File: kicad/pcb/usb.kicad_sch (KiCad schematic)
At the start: 13 parts, among them J1 USB_C_Receptacle, U1 FE1.1, Y1 Crystal_GND23

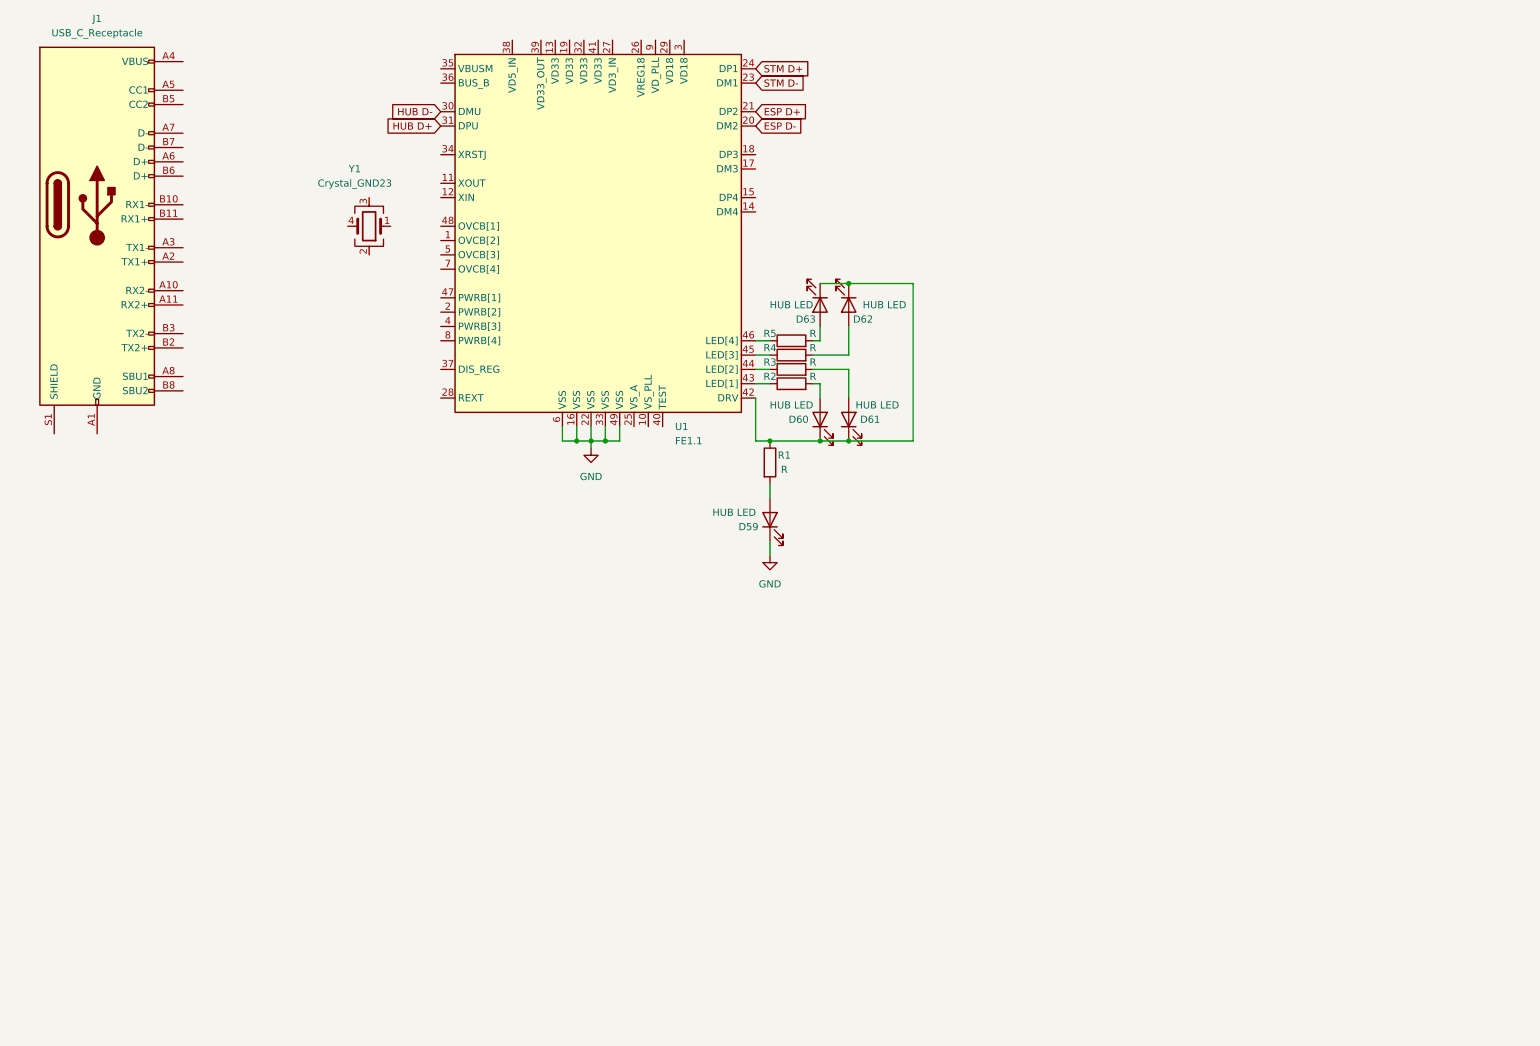
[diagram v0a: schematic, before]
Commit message: USB (almost) done + some STM progress
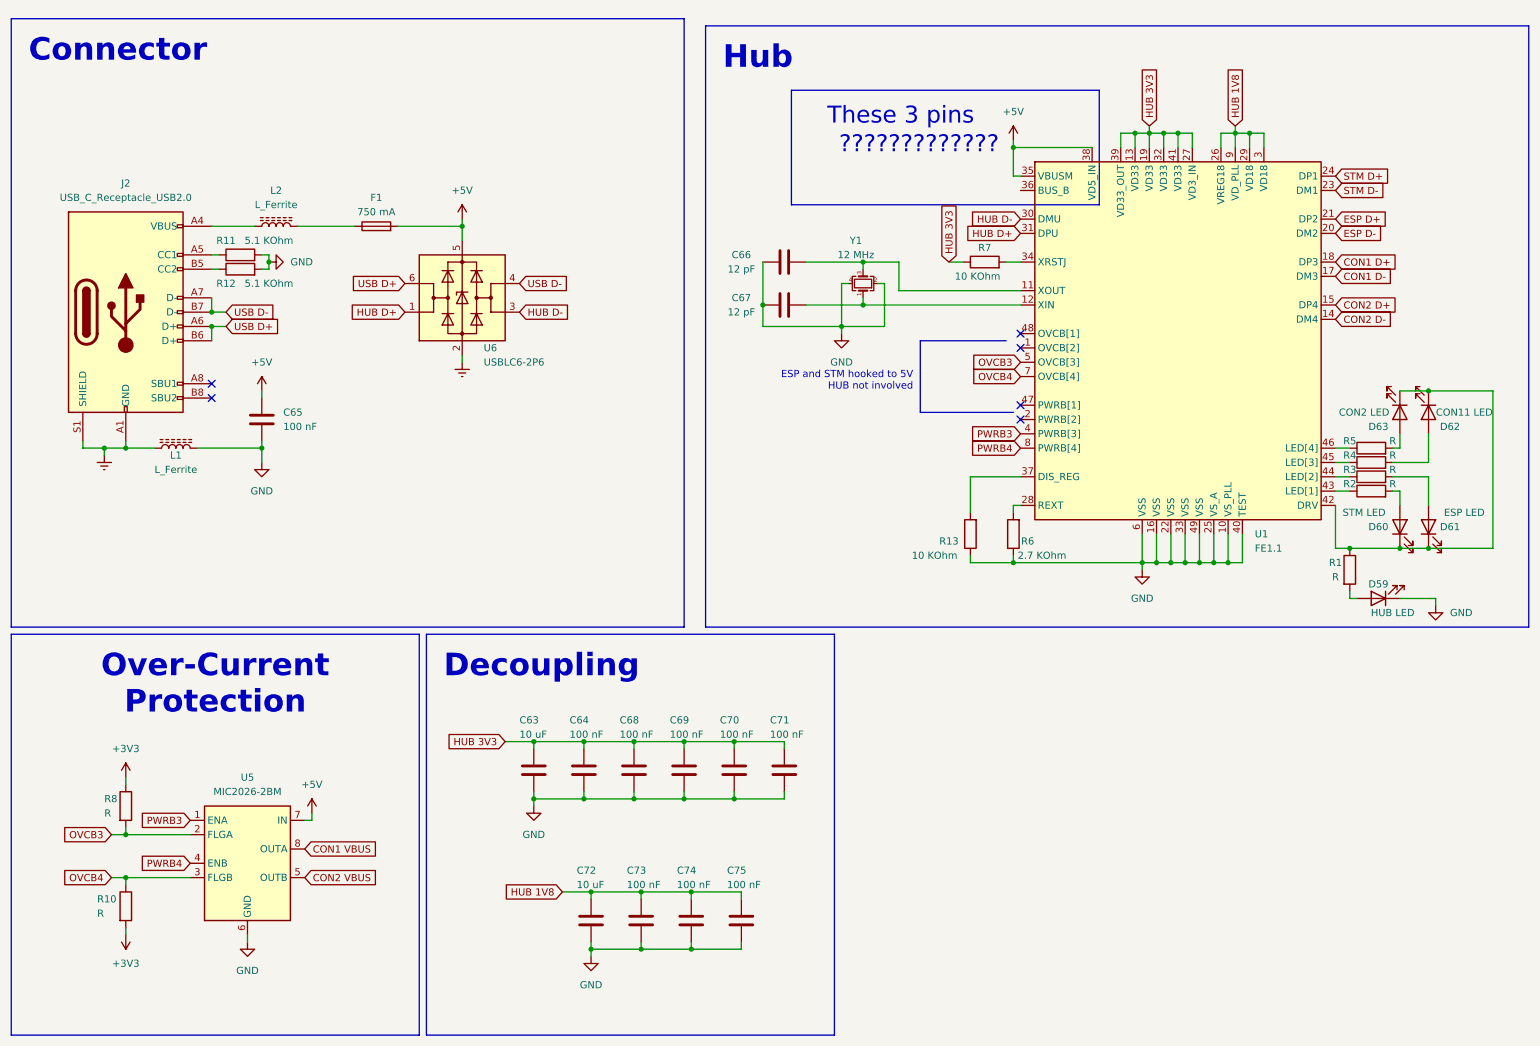
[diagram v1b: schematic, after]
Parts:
- removed J1: USB_C_Receptacle, symbol Connector:USB_C_Receptacle
- removed Y1: Crystal_GND23, symbol Device:Crystal_GND23
- added C63, C72: 10 uF, symbol Device:C
- added C64, C65, C68, C69, C70, C71, C73, C74, C75: 100 nF, symbol Device:C
- added C66, C67: 12 pF, symbol Device:C
- added F1: 750 mA, symbol Device:Fuse
- added J2: USB_C_Receptacle_USB2.0, symbol Connector:USB_C_Receptacle_USB2.0
- added L1, L2: L_Ferrite, symbol Device:L_Ferrite
- added R10, R8: R, symbol Device:R
- added R11, R12: 5.1 KOhm, symbol Device:R
- added R13, R7: 10 KOhm, symbol Device:R
- added R6: 2.7 KOhm, symbol Device:R
- added U5: MIC2026-2BM, Package_DIP:DIP-8_W7.62mm, symbol Power_Management:MIC2026-2BM
- added U6: USBLC6-2P6, Package_TO_SOT_SMD:SOT-666, symbol Power_Protection:USBLC6-2P6
- added Y1: 12 MHz, symbol Device:Crystal_GND24_Small
- D60: value HUB LED -> STM LED
- D61: value HUB LED -> ESP LED
- D62: value HUB LED -> CON11 LED
- D63: value HUB LED -> CON2 LED
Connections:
- net GND: now also U1.10 (VS_PLL), U1.25 (VS_A), U1.40 (TEST), C63.2, C64.2, C65.1, C66.1, C67.2, C68.2, C69.2, C70.2, C71.2, C72.2, C73.2, C74.2, C75.2, L1.2, R11.2, R12.2, R13.1, R6.1, U5.6 (GND), Y1.2, Y1.4
- net HUB D+: now also U6.1 (I/O1)
- net HUB D-: now also U6.3 (I/O2)
- net at U1.11 (XOUT): now also C66.2, Y1.3
- net at U1.12 (XIN): now also C67.1, Y1.1
- net HUB 3V3: now reaches U1.13 (VD33)
- net HUB 3V3: now also U1.19 (VD33), U1.27 (VD3_IN), U1.32 (VD33), U1.39 (VD33_OUT), U1.41 (VD33), C63.1, C64.1, C68.1, C69.1, C70.1, C71.1, R7.1
- net CON2 D-: now reaches U1.14 (DM4)
- net CON2 D+: now reaches U1.15 (DP4)
- net CON1 D-: now reaches U1.17 (DM3)
- net CON1 D+: now reaches U1.18 (DP3)
- net HUB 1V8: now reaches U1.26 (VREG18)
- net HUB 1V8: now also U1.29 (VD18), U1.3 (VD18), U1.9 (VD_PLL), C72.1, C73.1, C74.1, C75.1
- net at U1.28 (REXT): now also R6.2
- net at U1.34 (XRSTJ): now also R7.2
- net +5V: now reaches U1.35 (VBUSM)
- net +5V: now also U1.38 (VD5_IN), C65.2, F1.2, U5.7 (IN), U6.5 (VBUS)
- net at U1.37 (DIS_REG): now also R13.2
- net PWRB3: now reaches U1.4 (PWRB[3])
- net PWRB3: now also U5.1 (ENA)
- net OVCB3: now reaches U1.5 (OVCB[3])
- net OVCB3: now also R8.2, U5.2 (FLGA)
- net OVCB4: now reaches U1.7 (OVCB[4])
- net OVCB4: now also R10.1, U5.3 (FLGB)
- net PWRB4: now reaches U1.8 (PWRB[4])
- net PWRB4: now also U5.4 (ENB)
- new net: J2.B5 (CC2), R12.1
- new net: J2.A5 (CC1), R11.1
- new net: J2.A4 (VBUS), J2.A9 (VBUS), J2.B4 (VBUS), J2.B9 (VBUS), L2.1
- new net: F1.1, L2.2
- new net +3V3: R10.2, R8.1
- new net CON1 VBUS: U5.8 (OUTA)
- new net CON2 VBUS: U5.5 (OUTB)
- new net Earth: J2.A1 (GND), J2.A12 (GND), J2.B1 (GND), J2.B12 (GND), J2.S1 (SHIELD), L1.1, U6.2 (GND)
- new net USB D+: J2.A6 (D+), J2.B6 (D+), U6.6 (I/O1)
- new net USB D-: J2.A7 (D-), J2.B7 (D-), U6.4 (I/O2)
- no-connect marks 0 -> 6
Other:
- note added: "?????????????"
- note added: "ESP and STM hooked to 5V HUB not involved"
- note added: "These 3 pins"
- moved on the sheet: D59, D60, D61, D62, D63, R1, R2, R3, R4, R5, U1

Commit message: Initial support circuitry for STM and ESP
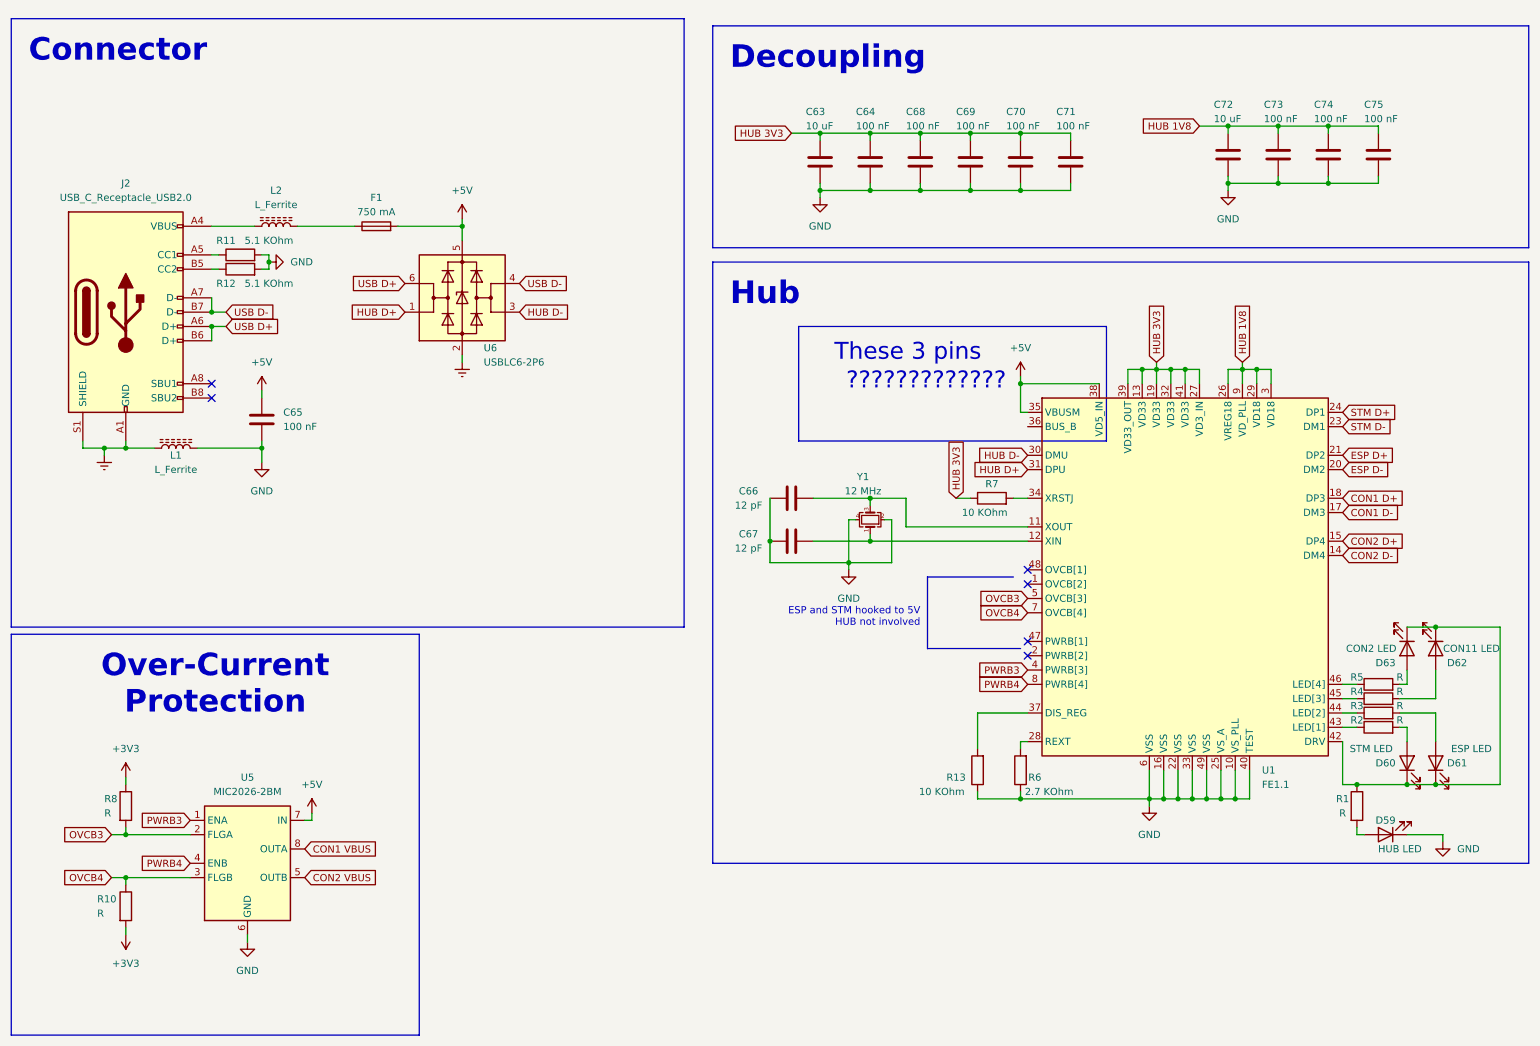
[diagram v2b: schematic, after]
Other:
- moved on the sheet: C63, C64, C66, C67, C68, C69, C70, C71, C72, C73, C74, C75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

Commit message: Hub wired(?) + STM and ESP may boot already
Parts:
- C63, C72: value 10 uF -> 10u; footprint (none) -> Capacitor_SMD:C_0402_1005Metric_Pad0.74x0.62mm_HandSolder
- C64, C65, C68, C69, C70, C71, C73, C74, C75: value 100 nF -> 100n; footprint (none) -> Capacitor_SMD:C_0402_1005Metric_Pad0.74x0.62mm_HandSolder
- C66, C67: value 12 pF -> 12p; footprint (none) -> Capacitor_SMD:C_0402_1005Metric_Pad0.74x0.62mm_HandSolder
- J2: value USB_C_Receptacle_USB2.0 -> USB Connector; footprint (none) -> PCM_marbastlib-various:USB_C_Receptacle_HRO_TYPE-C-31-M-12
- R1, R10, R2, R3, R4, R5, R8: footprint (none) -> Resistor_SMD:R_0402_1005Metric_Pad0.72x0.64mm_HandSolder
- R11, R12: value 5.1 KOhm -> 5K1; footprint (none) -> Resistor_SMD:R_0402_1005Metric_Pad0.72x0.64mm_HandSolder
- R13, R7: value 10 KOhm -> 10K; footprint (none) -> Resistor_SMD:R_0402_1005Metric_Pad0.72x0.64mm_HandSolder
- R6: value 2.7 KOhm -> 2K7; footprint (none) -> Resistor_SMD:R_0402_1005Metric_Pad0.72x0.64mm_HandSolder
- Y1: footprint (none) -> Crystal:Crystal_SMD_2016-4Pin_2.0x1.6mm
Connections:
- net CON1 VBUS: now also U5.5 (OUTB); no longer U5.8 (OUTA)
- net CON2 VBUS: now also U5.8 (OUTA); no longer U5.5 (OUTB)
- net ESP D+: now also U1.24 (DP1); no longer U1.21 (DP2)
- net ESP D-: now also U1.23 (DM1); no longer U1.20 (DM2)
- net OVCB3: now also R10.1, U5.3 (FLGB); no longer R8.2, U5.2 (FLGA)
- net OVCB4: now also R8.2, U5.2 (FLGA); no longer R10.1, U5.3 (FLGB)
- net PWRB3: now also U5.4 (ENB); no longer U5.1 (ENA)
- net PWRB4: now also U5.1 (ENA); no longer U5.4 (ENB)
- net STM D+: now also U1.21 (DP2); no longer U1.24 (DP1)
- net STM D-: now also U1.20 (DM2); no longer U1.23 (DM1)

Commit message: (WIP) Tracing v2
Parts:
- removed D60: STM LED, symbol Device:LED
- removed D61: ESP LED, symbol Device:LED
- removed D62: CON11 LED, symbol Device:LED
- removed D63: CON2 LED, symbol Device:LED
- removed R10, R2, R3, R4, R5, R8: R, Resistor_SMD:R_0402_1005Metric_Pad0.72x0.64mm_HandSolder, symbol Device:R
- removed U5: MIC2026-2BM, Package_DIP:DIP-8_W7.62mm, symbol Power_Management:MIC2026-2BM
- added C61: 10u, Capacitor_SMD:C_0402_1005Metric_Pad0.74x0.62mm_HandSolder, symbol Device:C
- added TP1 (x2), TP2 (x2): TestPoint, TestPoint:TestPoint_Pad_D2.0mm, symbol Connector:TestPoint
- D59: footprint (none) -> LED_SMD:LED_0402_1005Metric_Pad0.77x0.64mm_HandSolder
- F1: footprint (none) -> Fuse:Fuse_0402_1005Metric_Pad0.77x0.64mm_HandSolder
- L1, L2: footprint (none) -> Inductor_SMD:L_0402_1005Metric_Pad0.77x0.64mm_HandSolder
- Y1: footprint Crystal:Crystal_SMD_2016-4Pin_2.0x1.6mm -> Crystal:Crystal_SMD_3225-4Pin_3.2x2.5mm
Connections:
- net CON2 D+ is gone; now on net ESP D+: U1.15 (DP4)
- net CON2 D- is gone; now on net ESP D-: U1.14 (DM4)
- net OVCB3 is gone; now on net GND: U1.5 (OVCB[3])
- net OVCB4 is gone; now on net GND: U1.7 (OVCB[4])
- net PWRB4 is gone; now on net GND: U1.8 (PWRB[4])
- net +5V: now also C61.2
- net ESP D+: now also TP1.1; no longer U1.24 (DP1)
- net ESP D-: now also TP2.1; no longer U1.23 (DM1)
- net GND: now also U1.1 (OVCB[2]), U1.36 (BUS_B), U1.43 (LED[1]), U1.44 (LED[2]), U1.48 (OVCB[1]), C61.1; no longer U1.49 (VSS)
- net STM D+: now also U1.24 (DP1), TP1.1; no longer U1.21 (DP2)
- net STM D-: now also U1.23 (DM1), TP2.1; no longer U1.20 (DM2)
- net CON1 D+: no longer names the net of U1.18 (DP3)
- net CON1 D-: no longer names the net of U1.17 (DM3)
- net PWRB3: no longer names the net of U1.4 (PWRB[3])
- no-connect marks 6 -> 11
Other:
- note added: "Could maybe be left unconnected but datasheet's sample circuit hooked to GND"
- note removed: "?????????????"
- note removed: "ESP and STM hooked to 5V HUB not involved"
- note removed: "These 3 pins"
- moved on the sheet: D59, R1
